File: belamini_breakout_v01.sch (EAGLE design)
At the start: 5 parts, among them J1 M10SILK_FEMALE_PTH

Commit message: schematic components and layout
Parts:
- added A0J, A1J, A2J, A3J, A4J, A5J, A6J, A7J, ADC1, ADC2, ALOL, ALOR, DAC1, DAC2: WQP-PJ301M-12_JACK, thonkiconn:WQP-PJ301M-12_JACK
- added C1, C12, C15, C17, C19, C21, C23, C26, C3, C5, C7, C9: 1n, resistor:C-EUC0603
- added C10, C11, C13, C18, C2, C20, C22, C24, C25, C27, C28, C4, C6, C8: 10u, resistor:C-EUC0603
- added C14, C16: 100u, resistor:C-EUC0603
- added C29, C30, C31, C32, C33, C34: (no value), resistor:C-EUC0603
- added C35, C51: 100n, rcl:C-USC0603
- added C52, C53: 47u, rcl:CPOL-USD
- added D1, D2, D3, D4: WHITE, SparkFun-LED:LED-WHITE1206
- added D10, D9: 1N5819HW, diode:DIODE-SOD123
- added IC1, IC3, IC5: TL074D, linear:TL074D
- added IC10: LM4040B10, texas:LM4041B12DBZ
- added IC2: LM4041CIDBZ, texas:LM4041CIDBZ
- added J3, J4: (no value), SparkFun-Connectors:CONN_03
- added JP2: M05X2PTH, og-header:M05X2PTH
- added R1, R13, R18, R20, R24, R26, R33, R37, R41, R45, R5, R9: 3k3, resistor:R-EU_R0603
- added R10, R14, R19, R2, R22, R27, R28, R29, R30, R31, R32, R34, R38, R42, R46, R49, R50, R51, R56, R57, R6: 10k, resistor:R-EU_R0603
- added R11, R12, R15, R16, R17, R21, R3, R35, R36, R39, R4, R40, R43, R44, R47, R48, R7, R8: 100k, resistor:R-EU_R0603
- added R23, R25: 33k, resistor:R-EU_R0603
- added R52, R53, R54, R55: 470, resistor:R-EU_R0603
- added R58, R62: 470, rcl:R-US_R0603
- added S1, S2, S3, S4, S5, S6, S7, S8: MOMENTARY-SWITCH-SPST-SMD-6.2MM-TALL, SparkFun-Switches:MOMENTARY-SWITCH-SPST-SMD-6.2MM-TALL
- added SW1: EC12E_SW, switch-alps:EC12E_SW
- added VR1, VR10, VR11, VR12, VR2, VR3, VR4, VR9: 10k, SparkFun-Resistors:POTENTIOMETER-PTH-9MM-1/20W-20%-KIT
- U$1: value WQP-PJ301M-12_JACK -> RECOM785.0; device thonkiconn:WQP-PJ301M-12_JACK -> audioic:RECOM785.0
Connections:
- removed net 3V3: P1.14, P2.23
- new net +12V: C30.1, C31.1, C34.1, C52.+, D9.C, IC1P.V+, IC3P.V+, IC5P.V+, U$1.VIN
- new net +3V3: P1.14, P2.23, R27.2, R30.2, R31.2, R32.2, R49.2, R50.2, R51.2, R56.2, R57.2
- new net -10V: C51.1, IC10.A, R62.2, VR1.E, VR10.E, VR11.E, VR12.E, VR2.E, VR3.E, VR4.E, VR9.E
- new net -12V: C29.2, C32.2, C33.2, C53.-, D10.A, IC1P.V-, IC3P.V-, IC5P.V-, R62.1
- new net 1V2: C35.1, IC1A.+IN, IC1B.+IN, IC1C.+IN, IC1D.+IN, IC2.C, IC3A.+IN, IC3B.+IN, IC5A.+IN, IC5B.+IN, IC5C.+IN, IC5D.+IN, R58.2
- new net ADC1: C11.2, C12.2, IC3B.OUT, J3.3, R19.2
- new net ADC2: C10.2, C9.2, IC3A.OUT, J3.2, R22.2
- new net DAC1: J4.3, R24.1
- new net DAC2: J4.2, R26.1
- new net N$1: A0J.2, R3.1
- new net N$10: R11.2, R12.2, R9.1
- new net N$11: A1J.2, R11.1
- new net N$12: R12.1, VR3.S
- new net N$13: C7.1, IC1B.-IN, R13.2, R14.1
- new net N$14: R13.1, R15.2, R16.2
- new net N$15: A3J.2, R15.1
- new net N$16: R16.1, VR4.S
- new net N$17: C21.1, IC5C.-IN, R41.2, R42.1
- new net N$18: C19.1, IC5B.-IN, R37.2, R38.1
- new net N$19: C23.1, IC5D.-IN, R45.2, R46.1
- new net N$2: C1.1, IC1C.-IN, R1.2, R2.1
- new net N$20: ADC1.2, R17.1
- new net N$21: R17.2, R18.1
- new net N$22: C12.1, IC3B.-IN, R18.2, R19.1
- new net N$23: C9.1, IC3A.-IN, R20.2, R22.1
- new net N$24: C26.1, IC3C.-IN, R25.1, R26.2
- new net N$25: R20.1, R21.2
- new net N$26: ADC2.2, R21.1
- new net N$27: C14.2, DAC1.2
- new net N$28: C13.1, C14.1, C15.2, IC3D.OUT, R23.2
- new net N$29: C15.1, IC3D.-IN, R23.1, R24.2
- new net N$3: R1.1, R3.2, R4.2
- new net N$30: D4.A, R55.1
- new net N$31: C16.1, C25.1, C26.2, IC3C.OUT, R25.2
- new net N$32: C16.2, DAC2.2
- new net N$33: C17.1, IC5A.-IN, R33.2, R34.1
- new net N$34: R33.1, R35.2, R36.2
- new net N$35: A4J.2, R35.1
- new net N$36: R36.1, VR9.S
- new net N$37: D3.A, R54.1
- new net N$38: R37.1, R39.2, R40.2
- new net N$39: A5J.2, R39.1
- new net N$4: R4.1, VR1.S
- new net N$40: R40.1, VR10.S
- new net N$41: D2.A, R53.1
- new net N$42: R41.1, R43.2, R44.2
- new net N$43: A6J.2, R43.1
- new net N$44: R44.1, VR11.S
- new net N$45: D1.A, R52.1
- new net N$46: R45.1, R47.2, R48.2
- new net N$47: A7J.2, R47.1
- new net N$48: R48.1, VR12.S
- new net N$5: C3.1, IC1A.-IN, R5.2, R6.1
- new net N$52: D9.A, JP2.1, JP2.2
- new net N$53: D10.C, JP2.10, JP2.9
- new net N$6: R5.1, R7.2, R8.2
- new net N$7: A2J.2, R7.1
- new net N$8: R8.1, VR2.S
- new net N$9: C5.1, IC1D.-IN, R10.1, R9.2
- new net SCL: P2.9
- new net SDA: P2.11
- net 5V: now also R58.1, U$1.VOUT
- net A0: now also C1.2, C2.2, IC1C.OUT, R2.2
- net A1: now also C5.2, C6.2, IC1D.OUT, R10.2
- net A2: now also C3.2, C4.2, IC1A.OUT, R6.2
- net A3: now also C7.2, C8.2, IC1B.OUT, R14.2
- net A4: now also C17.2, C18.2, IC5A.OUT, R34.2
- net A5: now also C19.2, C20.2, IC5B.OUT, R38.2
- net A6: now also C21.2, C22.2, IC5C.OUT, R42.2
- net A7: now also C23.2, C24.2, IC5D.OUT, R46.2
- net D0: now also R55.2
- net D1: now also R54.2
- net D10: now also R30.1, S1.1
- net D11: now also R49.1, S4.1
- net D13: now also R27.1, SW1G$2.2
- net D14: now also C28.2, R29.2, SW1G$1.A
- net D15: now also C27.1, R28.1, SW1G$1.B
- net D2: now also R53.2
- net D3: now also R52.2
- net D4: now also R57.1, S8.1
- net D5: now also R56.1, S7.1
- net D6: now also R50.1, S5.1
- net D7: now also R51.1, S6.1
- net D8: now also R32.1, S3.1
- net D9: now also R31.1, S2.1
- net GND: now also A0J.1, A0J.3, A1J.1, A1J.3, A2J.1, A2J.3, A3J.1, A3J.3, A4J.1, A4J.3, A5J.1, A5J.3, A6J.1, A6J.3, A7J.1, A7J.3, ADC1.1, ADC1.3, ADC2.1, ADC2.3, C10.1, C11.1, C13.2, C18.1, C2.1, C20.1, C22.1, C24.1, C25.2, C27.2, C28.1, C29.1, C30.2, C31.2, C32.1, C33.1, C34.2, C35.2, C4.1, C51.2, C52.-, C53.+, C6.1, C8.1, D1.C, D2.C, D3.C, D4.C, DAC1.1, DAC2.1, DAC2.3, IC10.C, IC2.A, IC3C.+IN, IC3D.+IN, J3.1, J4.1, JP2.3, JP2.4, JP2.5, JP2.6, JP2.7, JP2.8, R28.2, R29.1, S1.2, S2.2, S3.2, S4.2, S5.2, S6.2, S7.2, S8.2, SW1G$1.C, SW1G$2.1, U$1.GND, VR1.A, VR10.A, VR11.A, VR12.A, VR2.A, VR3.A, VR4.A, VR9.A
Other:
- note added: "1mA"

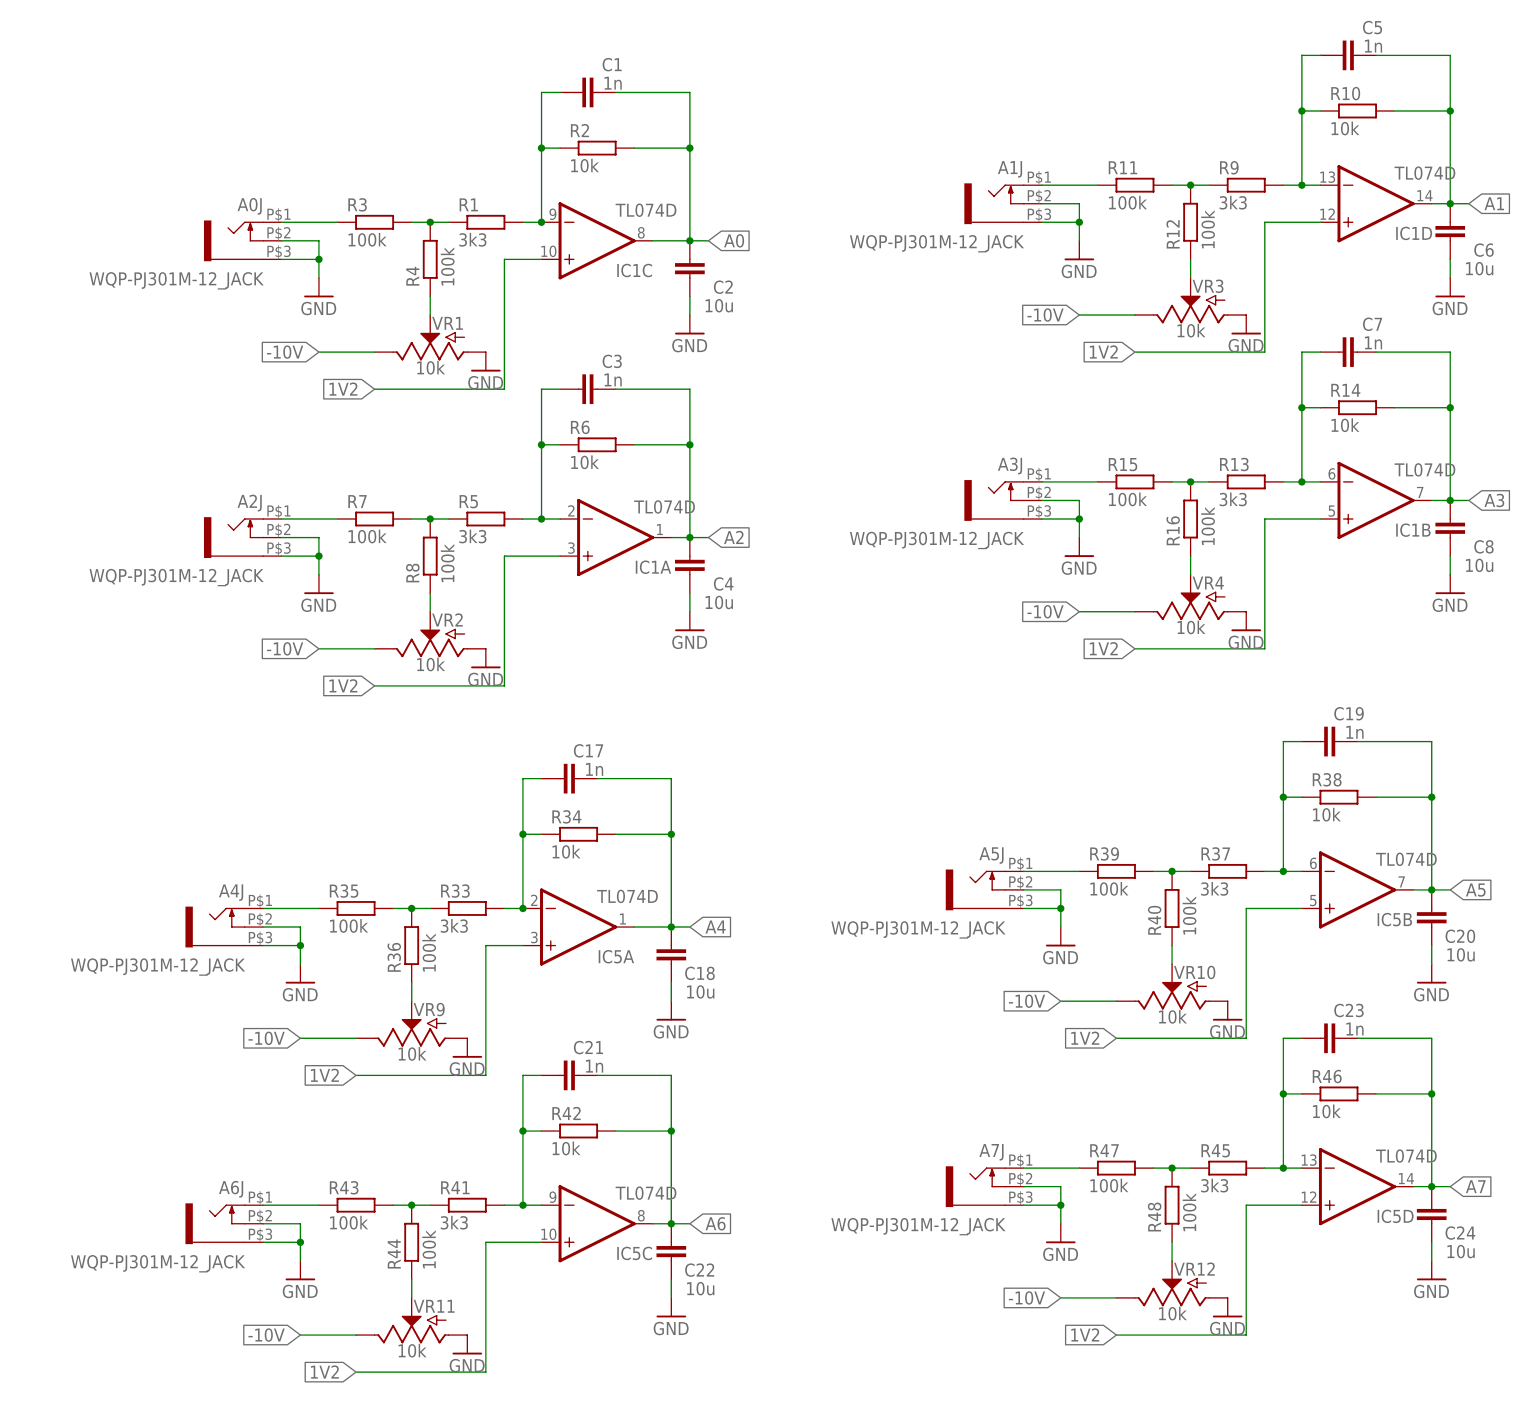
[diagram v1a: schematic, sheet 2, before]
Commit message: minimise features and layout
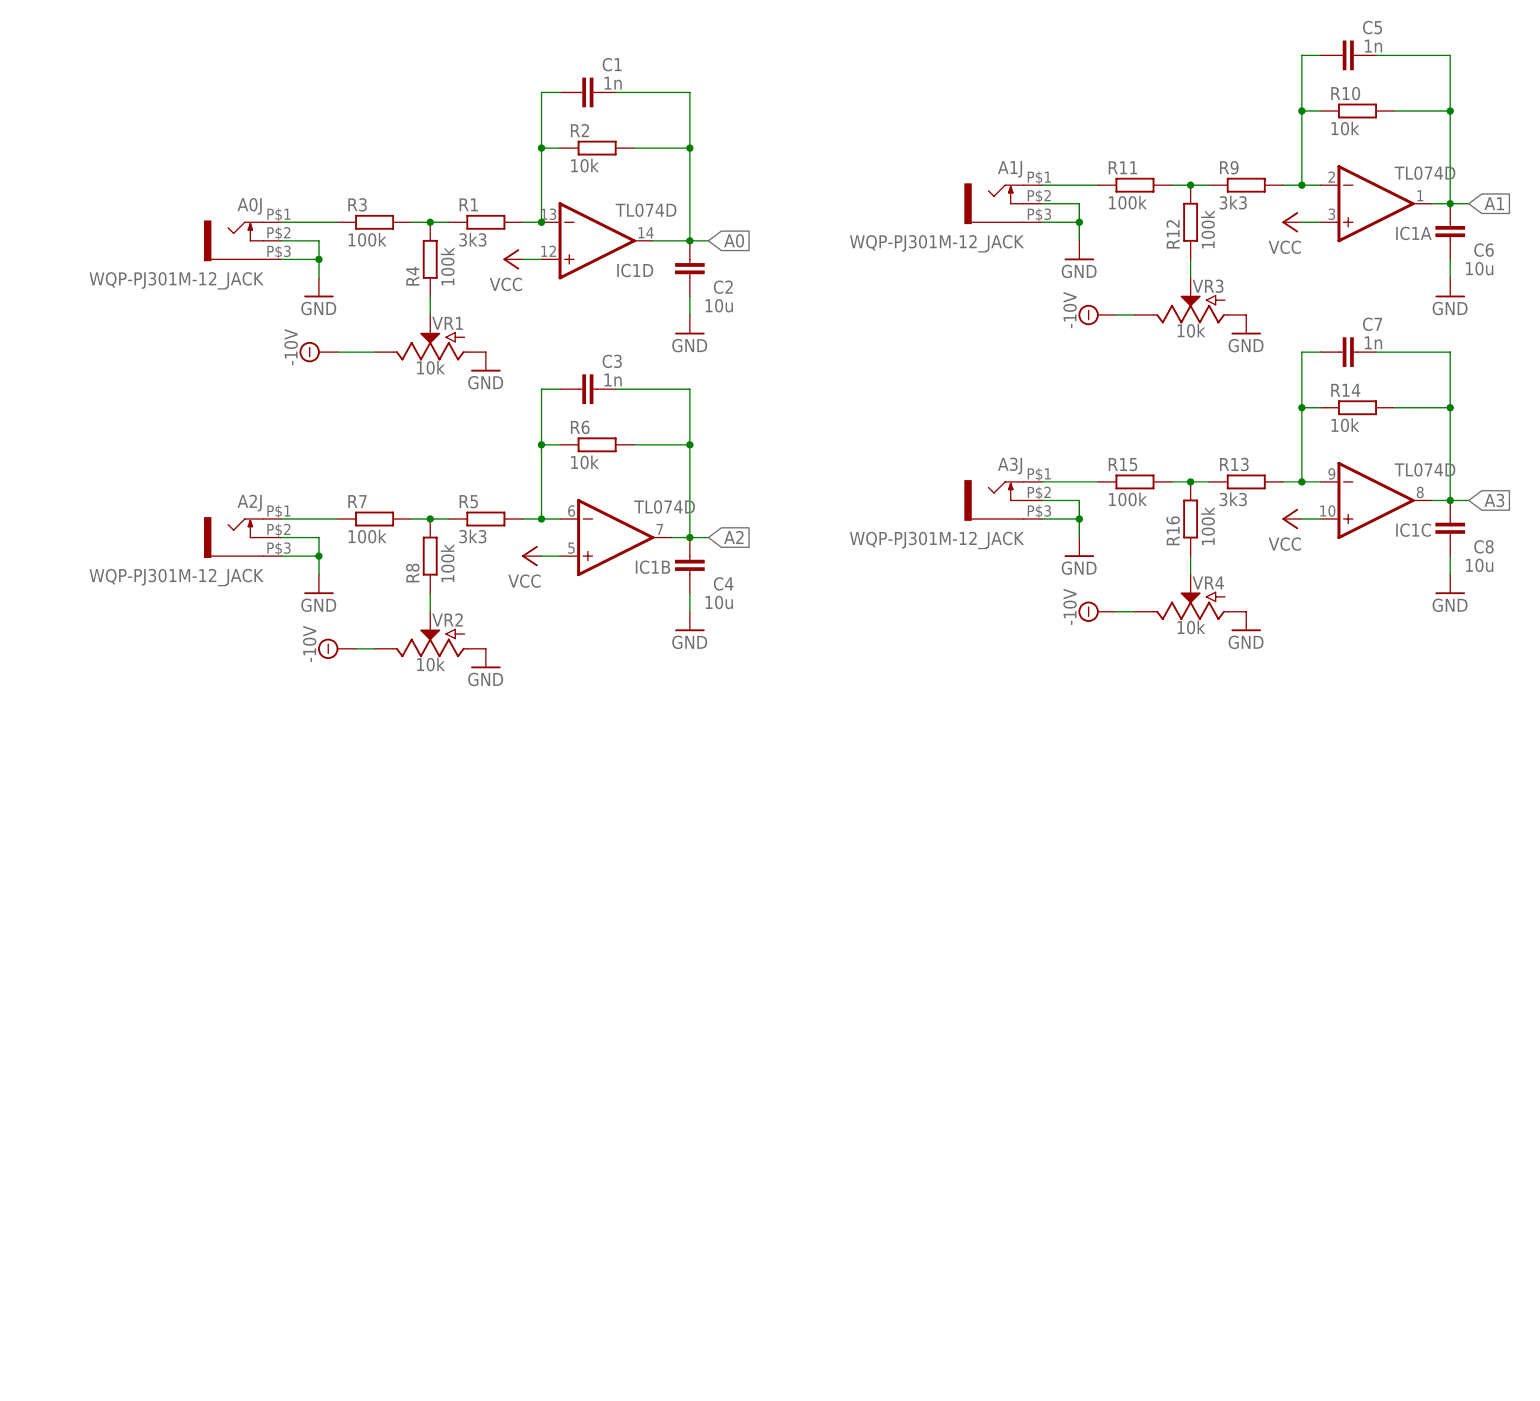
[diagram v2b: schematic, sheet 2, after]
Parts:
- removed A4J, A5J, A6J, A7J: WQP-PJ301M-12_JACK, thonkiconn:WQP-PJ301M-12_JACK
- removed C17, C19, C21, C23: 1n, resistor:C-EUC0603
- removed C18, C20, C22, C24: 10u, resistor:C-EUC0603
- removed C29, C30: (no value), resistor:C-EUC0603
- removed IC5: TL074D, linear:TL074D
- removed R33, R37, R41, R45: 3k3, resistor:R-EU_R0603
- removed R34, R38, R42, R46: 10k, resistor:R-EU_R0603
- removed R35, R36, R39, R40, R43, R44, R47, R48: 100k, resistor:R-EU_R0603
- removed VR10, VR11, VR12, VR9: 10k, SparkFun-Resistors:POTENTIOMETER-PTH-9MM-1/20W-20%-KIT
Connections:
- removed net 1V2: C35.1, IC1A.+IN, IC1B.+IN, IC1C.+IN, IC1D.+IN, IC2.C, IC3A.+IN, IC3B.+IN, IC5A.+IN, IC5B.+IN, IC5C.+IN, IC5D.+IN, R58.2
- removed net 5V: P1.24, R58.1, U$1.VOUT
- removed net N$17: C21.1, IC5C.-IN, R41.2, R42.1
- removed net N$18: C19.1, IC5B.-IN, R37.2, R38.1
- removed net N$19: C23.1, IC5D.-IN, R45.2, R46.1
- removed net N$33: C17.1, IC5A.-IN, R33.2, R34.1
- removed net N$34: R33.1, R35.2, R36.2
- removed net N$35: A4J.2, R35.1
- removed net N$36: R36.1, VR9.S
- removed net N$38: R37.1, R39.2, R40.2
- removed net N$39: A5J.2, R39.1
- removed net N$40: R40.1, VR10.S
- removed net N$42: R41.1, R43.2, R44.2
- removed net N$43: A6J.2, R43.1
- removed net N$44: R44.1, VR11.S
- removed net N$46: R45.1, R47.2, R48.2
- removed net N$47: A7J.2, R47.1
- removed net N$48: R48.1, VR12.S
- new net +5V: P1.24, U$1.VOUT
- new net VCC: C35.1, IC1A.+IN, IC1B.+IN, IC1C.+IN, IC1D.+IN, IC2.C, IC3A.+IN, IC3B.+IN, R58.2
- net +12V: no longer C30.1, IC5P.V+
- net +3V3: now also C27.2, C28.1, R58.1, SW1G$1.C
- net -10V: no longer VR10.E, VR11.E, VR12.E, VR9.E
- net -12V: no longer C29.2, IC5P.V-
- net A0: now also IC1D.OUT; no longer IC1C.OUT
- net A1: now also IC1A.OUT; no longer IC1D.OUT
- net A2: now also IC1B.OUT; no longer IC1A.OUT
- net A3: now also IC1C.OUT; no longer IC1B.OUT
- net A4: no longer C17.2, C18.2, IC5A.OUT, R34.2
- net A5: no longer C19.2, C20.2, IC5B.OUT, R38.2
- net A6: no longer C21.2, C22.2, IC5C.OUT, R42.2
- net A7: no longer C23.2, C24.2, IC5D.OUT, R46.2
- net ADC1: now also IC3A.OUT; no longer IC3B.OUT
- net ADC2: now also IC3B.OUT; no longer IC3A.OUT
- net D10: now also R56.1, S7.1; no longer R30.1, S1.1
- net D11: now also R57.1, S8.1; no longer R49.1, S4.1
- net D4: now also R30.1, S1.1; no longer R57.1, S8.1
- net D5: now also R31.1, S2.1; no longer R56.1, S7.1
- net D6: now also R32.1, S3.1; no longer R50.1, S5.1
- net D7: now also R49.1, S4.1; no longer R51.1, S6.1
- net D8: now also R50.1, S5.1; no longer R32.1, S3.1
- net D9: now also R51.1, S6.1; no longer R31.1, S2.1
- net GND: no longer A4J.1, A4J.3, A5J.1, A5J.3, A6J.1, A6J.3, A7J.1, A7J.3, C18.1, C20.1, C22.1, C24.1, C27.2, C28.1, C29.1, C30.2, SW1G$1.C, VR10.A, VR11.A, VR12.A, VR9.A
- net N$13: now also IC1C.-IN; no longer IC1B.-IN
- net N$2: now also IC1D.-IN; no longer IC1C.-IN
- net N$22: now also IC3A.-IN; no longer IC3B.-IN
- net N$23: now also IC3B.-IN; no longer IC3A.-IN
- net N$5: now also IC1B.-IN; no longer IC1A.-IN
- net N$9: now also IC1A.-IN; no longer IC1D.-IN
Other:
- moved on the sheet: IC1A, IC1B, IC1C, IC1D, IC3A, IC3B
